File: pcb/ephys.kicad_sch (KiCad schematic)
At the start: 7 parts, among them U1 RHS2116

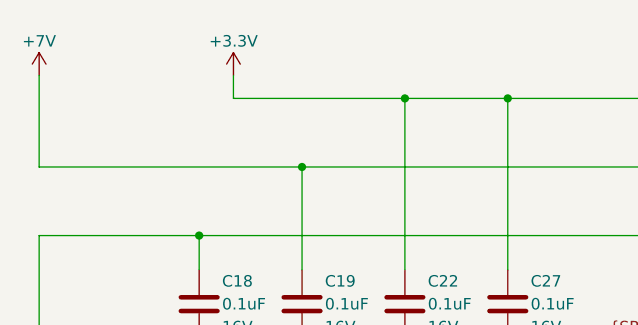
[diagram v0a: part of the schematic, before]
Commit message: Revision B
- Bring in changes from headstage-rhs116 rev. C that should make this design
  fully functional
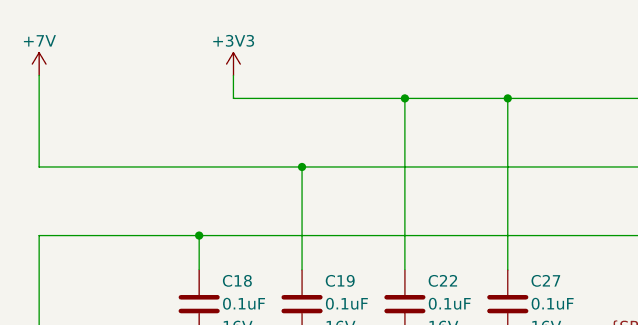
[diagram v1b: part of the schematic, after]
